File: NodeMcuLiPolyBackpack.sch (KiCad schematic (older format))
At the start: 14 parts, among them P1 Switch, P2 G BAT, P3 Battery, P4 5V, U1 MCP73831

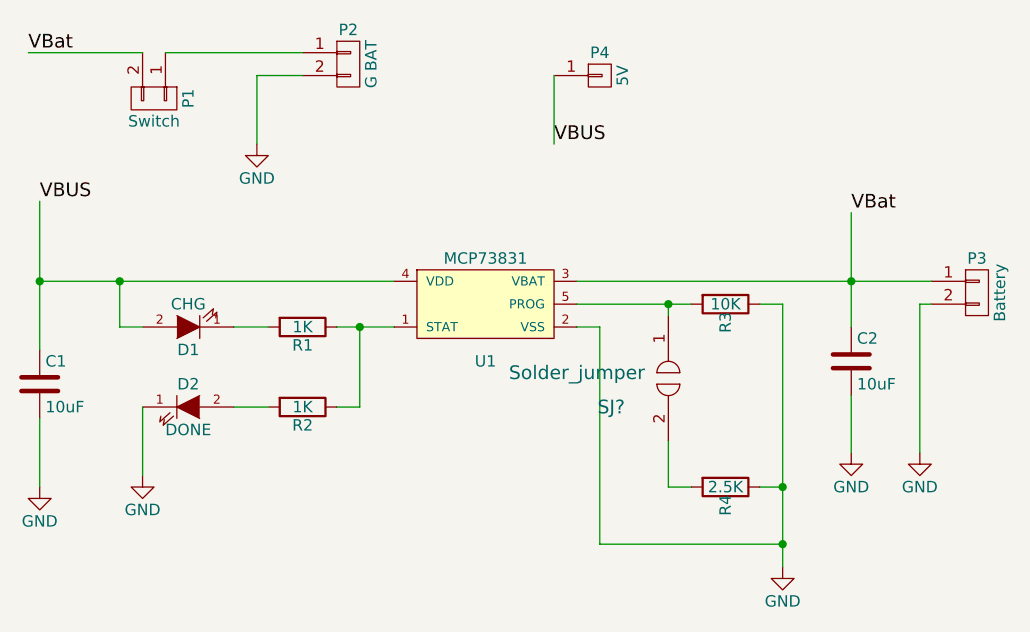
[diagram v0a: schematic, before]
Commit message: Fix connector, add PCB
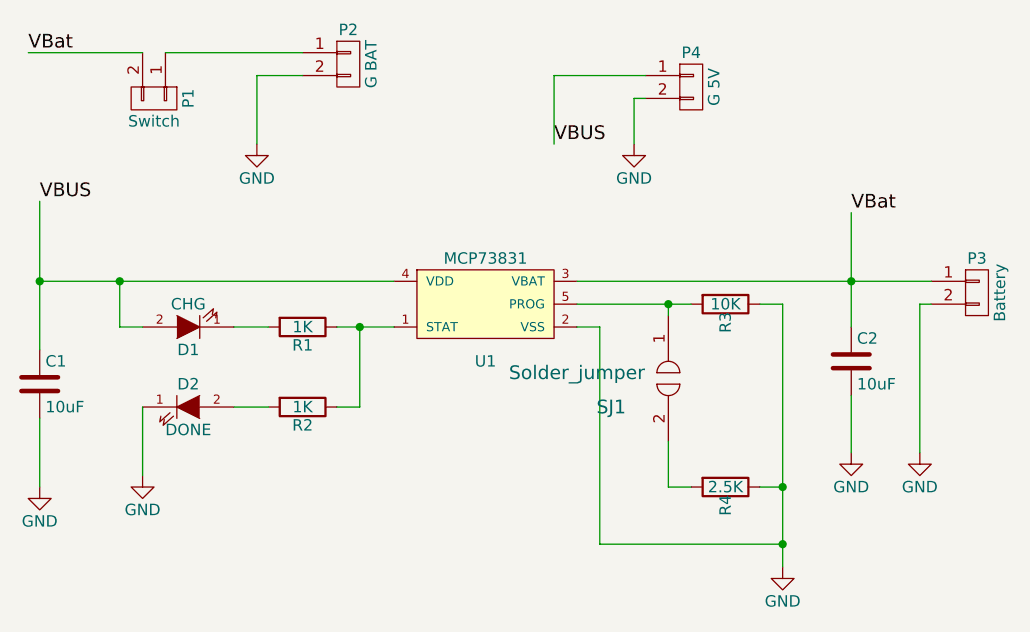
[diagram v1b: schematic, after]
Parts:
- removed P4: 5V, symbol CONN_01X01
- added P4: G 5V, Pin_Headers:Pin_Header_Straight_1x02, symbol CONN_01X02
- P2: footprint (none) -> Pin_Headers:Pin_Header_Straight_1x02
- SJ1: renamed from SJ?; footprint (none) -> open-project:S_JUMPER_2
- U1: footprint TO_SOT_Packages_SMD:SOT-23-5 -> Housings_SOT-23_SOT-143_TSOT-6:SOT-23-5
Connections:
- net GND: now also P4.2 (P2)
- net VBUS: now also P4.1 (P1)
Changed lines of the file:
@@
 F 0 "U1" H 4950 2600 50  0000 C CNN
 F 1 "MCP73831" H 4950 3050 50  0000 C CNN
-F 2 "TO_SOT_Packages_SMD:SOT-23-5" H 4950 2850 60  0001 C CNN
+F 2 "Housings_SOT-23_SOT-143_TSOT-6:SOT-23-5" H 4950 2850 60  0001 C CNN
 F 3 "" H 4950 2850 60  0000 C CNN
 	1    4950 2850
@@
 F 0 "P2" H 4350 1950 50  0000 C CNN
 F 1 "G BAT" V 4450 1800 50  0000 C CNN
-F 2 "" H 4350 1800 60  0000 C CNN
+F 2 "Pin_Headers:Pin_Header_Straight_1x02" H 4350 1800 60  0001 C CNN
 F 3 "" H 4350 1800 60  0000 C CNN
 	1    4350 1800
@@
 	5250 1850 5250 2150
 $Comp
-L CONN_01X01 P4
-U 1 1 5636E799
-P 5450 1850
-F 0 "P4" H 5450 1950 50  0000 C CNN
-F 1 "5V" V 5550 1850 50  0000 C CNN
-F 2 "" H 5450 1850 60  0000 C CNN
-F 3 "" H 5450 1850 60  0000 C CNN
-	1    5450 1850
-	1    0    0    -1
-$EndComp
-$Comp
-L Solder_jumper SJ?
+L Solder_jumper SJ1
 U 1 1 56381CC0
 P 5750 3200
-F 0 "SJ?" H 5500 3100 60  0000 C CNN
+F 0 "SJ1" H 5500 3100 60  0000 C CNN
 F 1 "Solder_jumper" H 5350 3250 60  0000 C CNN
-F 2 "" H 5350 3250 60  0000 C CNN
+F 2 "open-project:S_JUMPER_2" H 5350 3250 60  0001 C CNN
 F 3 "" H 5350 3250 60  0000 C CNN
 	1    5750 3200
@@
 	5450 3900 6250 3900
 Connection ~ 6250 3900
+$Comp
+L CONN_01X02 P4
+U 1 1 5638FFD1
+P 5850 1900
+F 0 "P4" H 5850 2050 50  0000 C CNN
+F 1 "G 5V" V 5950 1900 50  0000 C CNN
+F 2 "Pin_Headers:Pin_Header_Straight_1x02" H 5850 1900 60  0001 C CNN
+F 3 "" H 5850 1900 60  0000 C CNN
+	1    5850 1900
+	1    0    0    -1
+$EndComp
+Wire Wire Line
+	5250 1850 5650 1850
+$Comp
+L GND #PWR07
+U 1 1 5639011C
+P 5600 2150
+F 0 "#PWR07" H 5600 1900 50  0001 C CNN
+F 1 "GND" H 5600 2000 50  0000 C CNN
+F 2 "" H 5600 2150 60  0000 C CNN
+F 3 "" H 5600 2150 60  0000 C CNN
+	1    5600 2150
+	1    0    0    -1
+$EndComp
+Wire Wire Line
+	5650 1950 5600 1950
+Wire Wire Line
+	5600 1950 5600 2150
 $EndSCHEMATC
